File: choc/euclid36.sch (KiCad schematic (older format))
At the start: 104 parts, among them SW10 SW_PUSH, SW11 SW_PUSH, SW12 SW_PUSH, SW14 SW_PUSH, SW15 SW_PUSH, SW16 SW_PUSH, SW17 SW_PUSH, SW18 SW_PUSH, SW19 SW_PUSH, SW2 SW_PUSH, SW20 SW_PUSH, SW21 SW_PUSH, SW22 SW_PUSH, SW23 SW_PUSH, SW25 SW_PUSH, SW26 SW_PUSH, SW27 SW_PUSH, SW28 SW_PUSH, SW29 SW_PUSH, SW3 SW_PUSH, SW31 SW_PUSH, SW32 SW_PUSH, SW33 SW_PUSH, SW34 SW_PUSH, SW35 SW_PUSH, SW37 SW_PUSH, SW38 SW_PUSH, SW39 SW_PUSH, SW4 SW_PUSH, SW40 SW_PUSH, SW41 SW_PUSH, SW42 SW_PUSH, SW5 SW_PUSH, SW6 SW_PUSH, SW8 SW_PUSH, SW9 SW_PUSH, U2 ATmega32U4-MU, Y1 XTAL

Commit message: Small fixes
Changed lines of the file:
@@
 Text GLabel 2300 2850 2    50   Input ~ 0
 col4
-Text GLabel 2300 3050 0    50   Input ~ 0
+Text GLabel 2300 3050 2    50   Input ~ 0
 col5
 Text GLabel 2300 4050 2    50   Input ~ 0

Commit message: complete, ready for fabrication, though might change mini usb to micro usb before doing so
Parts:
- removed C5: 0.1u, Capacitor_SMD:C_0805_2012Metric_Pad1.18x1.45mm_HandSolder, symbol Device:C_Small
- removed D1: PRTR5V0U2X, euclid36-libs:SOT-143B, symbol Power_Protection:PRTR5V0U2X
- removed R3: 5.1k, Resistor_SMD:R_0805_2012Metric_Pad1.20x1.40mm_HandSolder, symbol Device:R_Small
- removed USB1: HRO-TYPE-C-31-M-12, euclid36-libs:HRO-TYPE-C-31-M-12-HandSoldering, symbol Type-C:HRO-TYPE-C-31-M-12
- added L14, L15, L16, L17, L18, L19, L20, L21, L22, L23, L24, L25, L26, L27, L28, L29, L30, L31, L32, L33, L34, L35, L36: WS2812B, euclid36-libs:SK6812-MINI-E, symbol reviung41-rescue:WS2812B-LED
- added USB1: Molex-0548190589, euclid36-libs:Molex-0548190589, symbol random-keyboard-parts:Molex-0548190589
- C1: value 1u -> 1uF; LCSC (none) -> C28323
- C2, C3, C4: value 0.1u -> 0.1uF; LCSC (none) -> C49678
- C5: renamed from C6; LCSC (none) -> C15850
- C7, C8: value 22p -> 22pF; LCSC (none) -> C520058
- D10, D11, D12, D14, D15, D16, D17, D18, D19, D2, D20, D21, D22, D23, D26, D27, D28, D29, D3, D31, D32, D33, D34, D35, D37, D38, D39, D4, D40, D41, D42, D5, D6, D8, D9: LCSC C81598 -> C727110
- F1: value Polyfuse_Small -> 500mA; footprint Fuse:Fuse_1206_3216Metric_Pad1.42x1.75mm_HandSolder -> Fuse:Fuse_1206_3216Metric; LCSC (none) -> C261942
- L1, L10, L11, L12, L13, L2, L3, L4, L5, L6, L7, L8, L9: footprint LED_SMD:LED_WS2812B_PLCC4_5.0x5.0mm_P3.2mm -> euclid36-libs:SK6812-MINI-E
- R1: footprint Resistor_SMD:R_0805_2012Metric_Pad1.20x1.40mm_HandSolder -> Resistor_SMD:R_0805_2012Metric; LCSC (none) -> C17414
- R2: value 5.1k -> 10k; footprint Resistor_SMD:R_0805_2012Metric_Pad1.20x1.40mm_HandSolder -> Resistor_SMD:R_0805_2012Metric; LCSC (none) -> C17414
- R4, R5: value R_Small -> 22; footprint Resistor_SMD:R_0805_2012Metric_Pad1.20x1.40mm_HandSolder -> Resistor_SMD:R_0805_2012Metric; LCSC (none) -> C17561
- SW10, SW11, SW12, SW14, SW15, SW16, SW17, SW18, SW19, SW2, SW20, SW21, SW22, SW23, SW25, SW26, SW27, SW28, SW29, SW3, SW31, SW32, SW33, SW34, SW35, SW37, SW38, SW39, SW4, SW40, SW41, SW42, SW5, SW6, SW8, SW9: footprint euclid36-libs:KailhChoc-1U -> euclid36-libs:Kailh_socket_PG1350
- U2: value ATmega32U4-MU -> ATmega32U4-AU; footprint Package_DFN_QFN:QFN-44-1EP_7x7mm_P0.5mm_EP5.2x5.2mm -> Package_QFP:TQFP-44_10x10mm_P0.8mm; symbol MCU_Microchip_ATmega:ATmega32U4-MU -> MCU_Microchip_ATmega:ATmega32U4-AU; LCSC (none) -> C44854
- Y1: footprint Crystal:Crystal_SMD_3225-4Pin_3.2x2.5mm_HandSoldering -> Crystal:Crystal_SMD_3225-4Pin_3.2x2.5mm; LCSC (none) -> C13738
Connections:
- net +5V: now also R2.1, U2.7 (VBUS), USB1.1 (GND)
- net GND: now also L14.3 (VSS), L15.3 (VSS), L16.3 (VSS), L17.3 (VSS), L18.3 (VSS), L19.3 (VSS), L20.3 (VSS), L21.3 (VSS), L22.3 (VSS), L23.3 (VSS), L24.3 (VSS), L25.3 (VSS), L26.3 (VSS), L27.3 (VSS), L28.3 (VSS), L29.3 (VSS), L30.3 (VSS), L31.3 (VSS), L32.3 (VSS), L33.3 (VSS), L34.3 (VSS), L35.3 (VSS), L36.3 (VSS); no longer R2.2, U2.45 (GND)
- net LED: no longer U2.9 (PB1)
- net VCC: now also L14.1 (VDD), L15.1 (VDD), L16.1 (VDD), L17.1 (VDD), L18.1 (VDD), L19.1 (VDD), L20.1 (VDD), L21.1 (VDD), L22.1 (VDD), L23.1 (VDD), L24.1 (VDD), L25.1 (VDD), L26.1 (VDD), L27.1 (VDD), L28.1 (VDD), L29.1 (VDD), L30.1 (VDD), L31.1 (VDD), L32.1 (VDD), L33.1 (VDD), L34.1 (VDD), L35.1 (VDD), L36.1 (VDD), USB1.5 (VBUS)
- net col0: now also U2.36 (PF7); no longer U2.28 (PB4)
- net col1: now also U2.37 (PF6); no longer U2.29 (PB5)
- net col2: now also U2.38 (PF5); no longer U2.30 (PB6)
- net col3: now also U2.39 (PF4); no longer U2.31 (PC6)
- net col4: now also U2.40 (PF1); no longer U2.32 (PC7)
- net col5: now also U2.41 (PF0); no longer U2.18 (PD0)
- net reset: now also R2.2
- net row0: now also U2.10 (PB2); no longer U2.1 (PE6)
- net row1: now also U2.9 (PB1); no longer U2.41 (PF0)
- net row2: now also U2.8 (PB0); no longer U2.40 (PF1)
- net row3: now also U2.25 (PD4); no longer U2.39 (PF4)
- net row4: now also U2.26 (PD6); no longer U2.38 (PF5)
- net row5: now also U2.27 (PD7); no longer U2.37 (PF6)
- net row6: now also U2.32 (PC7); no longer U2.36 (PF7)
- net at L13.2 (DOUT): now also L14.4 (DIN)
- net at R4.2: now also USB1.4 (D-)
- net at R5.2: now also USB1.3 (D+)
- new net: L14.2 (DOUT), L15.4 (DIN)
- new net: L15.2 (DOUT), L16.4 (DIN)
- new net: L16.2 (DOUT), L17.4 (DIN)
- new net: L17.2 (DOUT), L18.4 (DIN)
- new net: L18.2 (DOUT), L19.4 (DIN)
- new net: L19.2 (DOUT), L20.4 (DIN)
- new net: L20.2 (DOUT), L21.4 (DIN)
- new net: L21.2 (DOUT), L22.4 (DIN)
- new net: L22.2 (DOUT), L23.4 (DIN)
- new net: L23.2 (DOUT), L24.4 (DIN)
- new net: L24.2 (DOUT), L25.4 (DIN)
- new net: L25.2 (DOUT), L26.4 (DIN)
- new net: L27.2 (DOUT), L28.4 (DIN)
- new net: L26.2 (DOUT), L27.4 (DIN)
- new net: L28.2 (DOUT), L29.4 (DIN)
- new net: L29.2 (DOUT), L30.4 (DIN)
- new net: L30.2 (DOUT), L31.4 (DIN)
- new net: L31.2 (DOUT), L32.4 (DIN)
- new net: L32.2 (DOUT), L33.4 (DIN)
- new net: L33.2 (DOUT), L34.4 (DIN)
- new net: L34.2 (DOUT), L35.4 (DIN)
- new net: L35.2 (DOUT), L36.4 (DIN)
- no-connect marks 4 -> 2
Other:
- moved on the sheet: C2, C3, C4, C5, L1, L10, L11, L12, L13, L2, L3, L4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

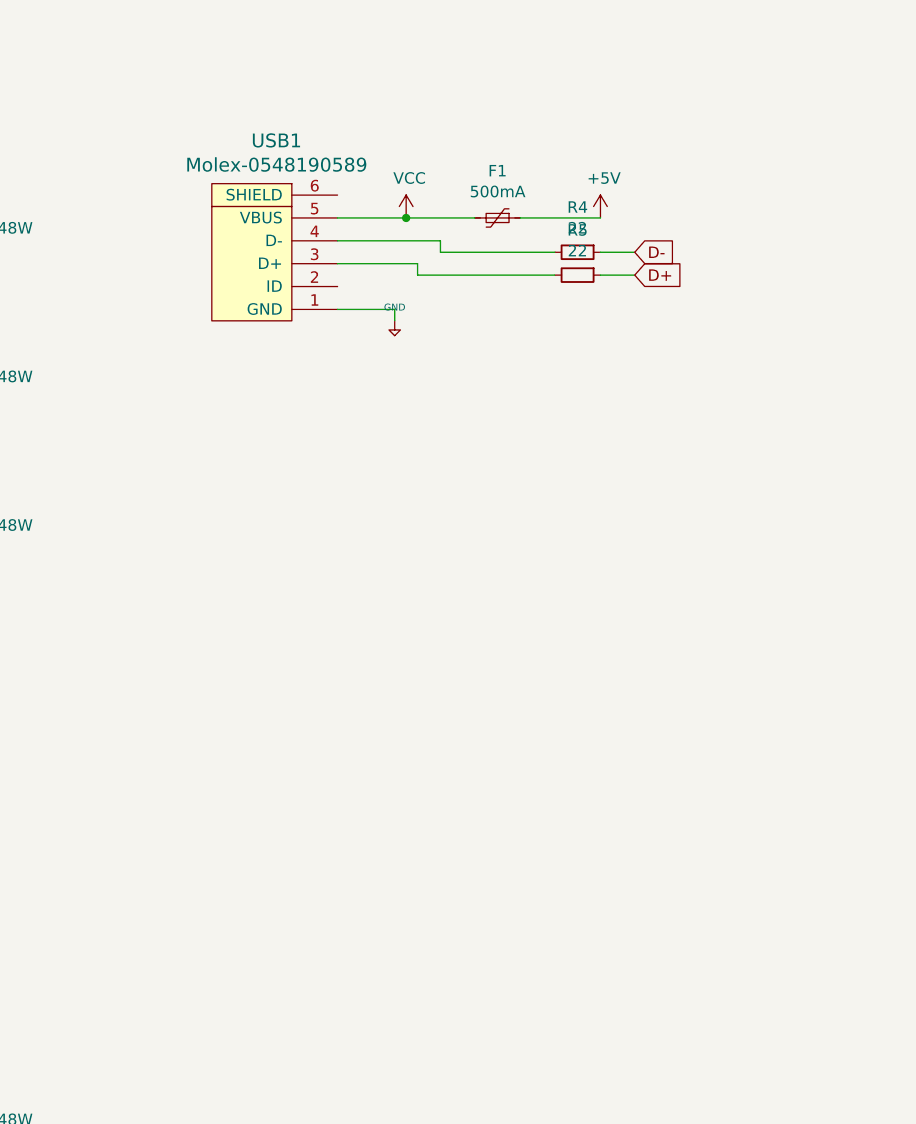
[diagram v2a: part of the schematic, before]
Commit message: Updated choc version to use usb-c. Almost done, still need to create a case / svgs
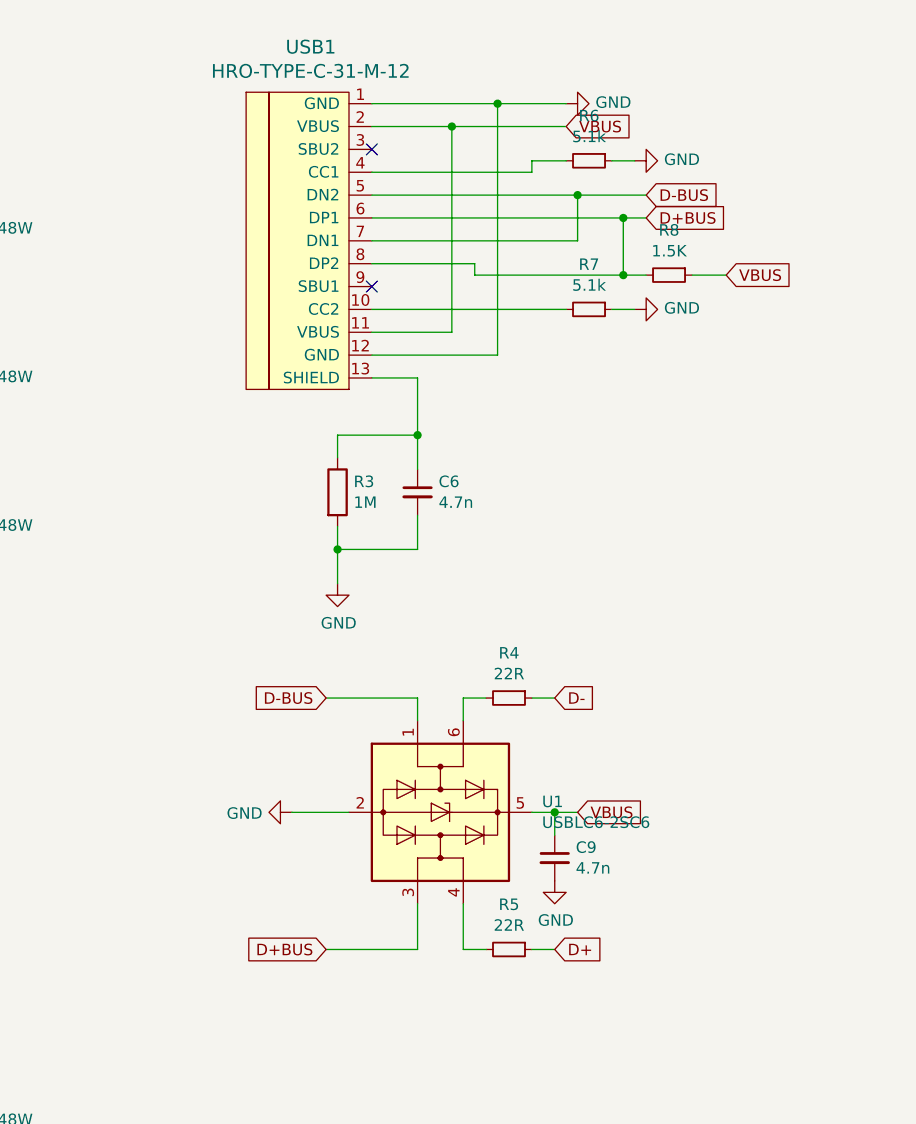
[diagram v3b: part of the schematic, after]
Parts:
- removed F1: 500mA, Fuse:Fuse_1206_3216Metric, symbol Device:Polyfuse_Small
- removed USB1: Molex-0548190589, euclid36-libs:Molex-0548190589, symbol random-keyboard-parts:Molex-0548190589
- added C6, C9: 4.7n, Capacitor_SMD:C_0805_2012Metric, symbol Device:C_Small
- added R3: 1M, Resistor_SMD:R_0805_2012Metric, symbol Device:R
- added R6, R7: 5.1k, Resistor_SMD:R_0805_2012Metric, symbol Device:R_Small
- added R8: 1.5K, Resistor_SMD:R_0805_2012Metric, symbol Device:R_Small
- added U1: USBLC6-2SC6, Package_TO_SOT_SMD:SOT-23-6, symbol Power_Protection:USBLC6-2SC6
- added USB1: HRO-TYPE-C-31-M-12, euclid36-libs:HRO-TYPE-C-31-M-12-Assembly, symbol Type-C:HRO-TYPE-C-31-M-12
- R4, R5: value 22 -> 22R
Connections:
- net GND: now also C6.2, C9.2, R3.2, R6.1, R7.1, U1.2 (GND), USB1.1 (GND), USB1.12 (GND)
- net at R4.2: now also U1.6 (I/O1)
- net at R5.2: now also U1.4 (I/O2)
- new net: R7.2, USB1.10 (CC2)
- new net: C6.1, R3.1, USB1.13 (SHIELD)
- new net: R6.2, USB1.4 (CC1)
- new net D+BUS: R8.2, U1.3 (I/O2), USB1.6 (DP1), USB1.8 (DP2)
- new net D-BUS: U1.1 (I/O1), USB1.5 (DN2), USB1.7 (DN1)
- new net VBUS: C9.1, R8.1, U1.5 (VBUS), USB1.11 (VBUS), USB1.2 (VBUS)
- no-connect marks 2 -> 4

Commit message: Updated to include mounting holes and gerber update
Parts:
- U2: footprint Package_QFP:TQFP-44_10x10mm_P0.8mm -> euclid36-libs:ATMEGA32U4-AU; symbol MCU_Microchip_ATmega:ATmega32U4-AU -> MCU_Microchip_ATmega:ATmega32U4-A
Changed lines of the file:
@@
 	2650 3950 2750 3950
 $Comp
-L MCU_Microchip_ATmega:ATmega32U4-AU U2
+L MCU_Microchip_ATmega:ATmega32U4-A U2
 U 1 1 6066A810
 P 1700 3350
 F 0 "U2" H 1700 1461 50  0000 C CNN
 F 1 "ATmega32U4-AU" H 1700 1370 50  0000 C CNN
-F 2 "Package_QFP:TQFP-44_10x10mm_P0.8mm" H 1700 3350 50  0001 C CIN
+F 2 "euclid36-libs:ATMEGA32U4-AU" H 1700 3350 50  0001 C CIN
 F 3 "http://ww1.microchip.com/downloads/en/DeviceDoc/Atmel-7766-8-bit-AVR-ATmega16U4-32U4_Datasheet.pdf" H 1700 3350 50  0001 C CNN
 F 4 "C44854" H 1700 3350 50  0001 C CNN "LCSC"

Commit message: latest low pro choc keyboard
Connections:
- net LED: now also U2.11 (PB3)
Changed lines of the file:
@@
 Text GLabel 1100 1850 0    50   Input ~ 0
 reset
-Text GLabel 2450 1350 2    50   Input ~ 0
+Text GLabel 2300 2150 2    50   Input ~ 0
 LED
 $Comp
